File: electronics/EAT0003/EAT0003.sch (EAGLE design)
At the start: 42 parts, among them IC1 LM2596S, J1 CONN-OSTTE1201X4, J2 CONN-RECT-16PIN-2ROWSIDE, Q1 MMBT3904, U1 24AA014, U2 MIC5205, U3 LM317KTTR, U4 H11F1SM

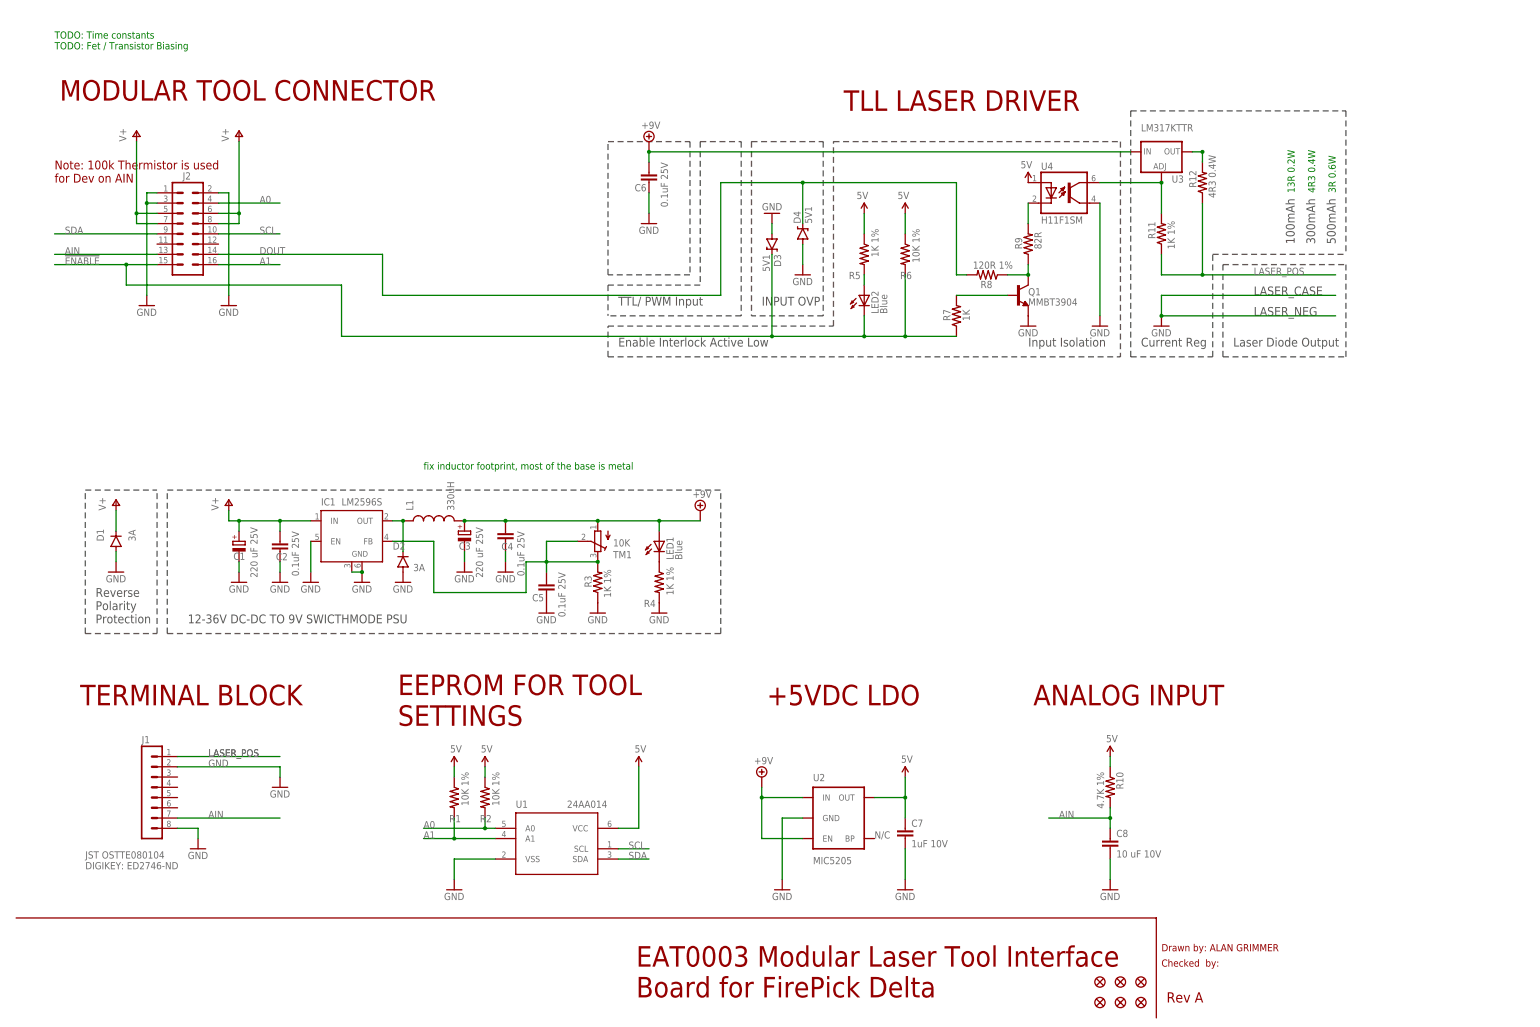
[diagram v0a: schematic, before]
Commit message: Laser Schematic + PCB Update
Added 30 mm fan mounts + connector
Changed values to suit mods on prototype
Added switchmode PSU enable line to global enable line to stop current
flowing
Added more TODO:'s to schematic
Added copper pours on both sides of PCB
Un mirrored PCB
Added logo's, part number, fiducials back in
Changed LM317 to correct footprint
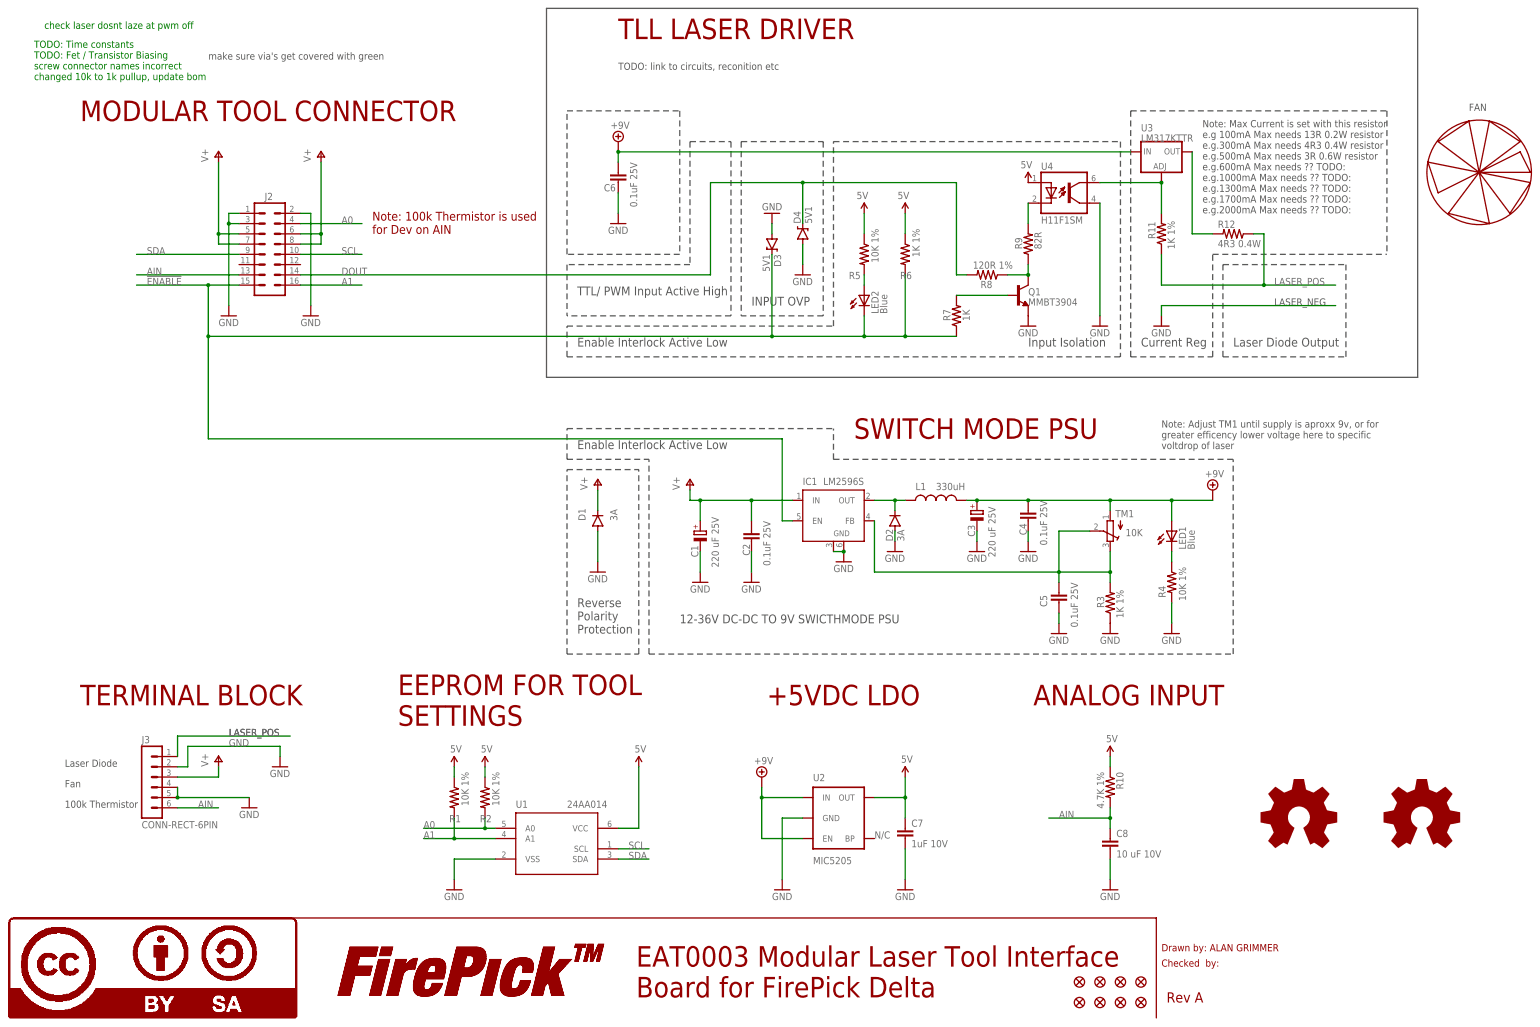
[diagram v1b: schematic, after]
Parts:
- removed J1: CONN-OSTTE1201X4, FirePick:CONN-OSTTE1201X4
- added FAN1: FAN_30MM, fan:FAN_30MM
- added FID7, FID8: FIDUCIAL1X2, SparkFun-Aesthetics:FIDUCIAL1X2
- added J3: CONN-RECT-6PIN, CONN_FPD:CONN-RECT-6PIN
- added LOGO1, LOGO5: LOGO-CC-BY-SASMALL, FirePick:LOGO-CC-BY-SASMALL
- added LOGO2, LOGO6: LOGO-FIREPICKSMALL, FirePick:LOGO-FIREPICKSMALL
- added LOGO3, LOGO4: LOGO-OSHWSMALL, FirePick:LOGO-OSHWSMALL
- R4, R5: value 1K 1% -> 10K 1%
- R6: value 10K 1% -> 1K 1%
- U3: device SparkFun-PowerIC:V_REG_317DPACK -> LM317:V_REG_317
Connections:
- net !ENABLE: now also IC1.EN
- net AIN: now also J3.6; no longer J1.7
- net GND: now also J3.2, J3.4, J3.5; no longer IC1.EN, J1.2, J1.8
- net LASER_POS: now also J3.1; no longer J1.1
- net V+: now also J3.3
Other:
- note added: "100k Thermistor"
- note added: "FAN"
- note added: "Fan"
- note added: "Laser Diode"
- note added: "Note: Adjust TM1 until supply is aproxx 9v, or for greater efficency lower voltage here to specific voltdrop of laser"
- note added: "Note: Max Current is set with this resistor e.g 100mA Max needs 13R 0.2W resistor e.g.300mA Max needs 4R3 0.4W resistor e.g.500mA Max needs 3R 0.6W resistor e.g.600mA Max needs ?? TODO: e.g.1000mA Max needs ?? TODO: e.g.1300mA Max needs ?? TODO: e.g.1700mA Max needs ?? TODO: e.g.2000mA Max needs ?? TODO:"
- note added: "SWITCH MODE PSU"
- note added: "TODO: Time constants TODO: Fet / Transistor Biasing screw connector names incorrect changed 10k to 1k pullup, update bom"
- note added: "TODO: link to circuits, reconition etc"
- note added: "TTL/ PWM Input Active High"
- note added: "check laser dosnt laze at pwm off"
- note added: "make sure via's get covered with green"
- note removed: "100mAh"
- note removed: "13R 0.2W"
- note removed: "300mAh"
- note removed: "3R 0.6W"
- note removed: "4R3 0.4W"
- note removed: "500mAh"
- note removed: "JST OSTTE080104 DIGIKEY: ED2746-ND"
- note removed: "LASER_CASE"
- note removed: "TODO: Time constants TODO: Fet / Transistor Biasing"
- note removed: "TTL/ PWM Input"
- note removed: "fix inductor footprint, most of the base is metal"
- moved on the sheet: C1, C2, C3, C4, C5, C6, D1, D2, IC1, J2, L1, LED1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

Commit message: Further schematic updates
- updated comments on schematic
- added credit to crow + license terms
- generated pdf's
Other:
- note added: "Fan is for optional cooling of LM317"
- note added: "License - This schematic is licensed under Creative Commons Attribution-ShareAlike (CC BY-SA)(https://creativecommons.org/licenses/by-sa/4.0/legalcode). Commercial use is OK, but you are required under the license conditions to share your changes with the internet, and also credit Crow's schematic ((http://www.repairfaq.org/sam/laserdps.htm#dpsldd317)"
- note added: "Note: 100k Thermistor is used to monitor the temperature on the laser diode heatsink on AIN"
- note added: "Note: Adjust TM1 until supply is aproxx 9v, or for greater efficency(less heat) lower voltage here to the specific voltdrop of laserdiode. remember the volt drop changes depending on the current thru the laser diode"
- note added: "Note: Max Current is set with this resistor e.g 100mA Max needs 13R 0.2W resistor e.g.300mA Max needs 4R3 0.4W resistor e.g.500mA Max needs 3R 0.6W resistor e.g.600mA Max needs 2R4 0.7W resistor e.g.1000mA Max needs 1R5 1.1W resistor e.g.1300mA Max needs 1R 1.6W resistor e.g.1700mA Max needs 0R75 2.1W resistor"
- note added: "Original credit goes to Crow for his schematic from here (http://www.repairfaq.org/sam/laserdps.htm#dpsldd317) Crow also came up with the modified circuit below to get an enable line and some isolation in, and removing opamp for TTL only to save cost Crow aslo agree to license this under the same license Fire Pick Delta uses"
- note added: "TODO's"
- note added: "This switchmode is required to drop the voltage for the laser driver, with out this it would end up as heat and the linear constant current source LM317 would melt its self of the board"
- note added: "changed 10k to 1k pullup, update bom"
- note added: "look at adding key switch to lock out use"
- note removed: "Note: 100k Thermistor is used for Dev on AIN"
- note removed: "Note: Adjust TM1 until supply is aproxx 9v, or for greater efficency lower voltage here to specific voltdrop of laser"
- note removed: "Note: Max Current is set with this resistor e.g 100mA Max needs 13R 0.2W resistor e.g.300mA Max needs 4R3 0.4W resistor e.g.500mA Max needs 3R 0.6W resistor e.g.600mA Max needs ?? TODO: e.g.1000mA Max needs ?? TODO: e.g.1300mA Max needs ?? TODO: e.g.1700mA Max needs ?? TODO: e.g.2000mA Max needs ?? TODO:"
- note removed: "TODO: Time constants TODO: Fet / Transistor Biasing screw connector names incorrect changed 10k to 1k pullup, update bom"
- note removed: "TODO: link to circuits, reconition etc"
- moved on the sheet: C1, C2, C3, C4, C5, C6, D1, D2, D3, D4, IC1, L1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
